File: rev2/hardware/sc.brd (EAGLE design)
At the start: 65 x 56 mm, 81 parts, among them IC1 PB137ACV, IC2 LM2675M-ADJ, Q1 si2305cd, Q2 IRFR5305, Q3 IRFR5305, T1 BC846, U1 SPX5205 3v3, X3 MKDSN1,5/4-5,08, X4 ts, X5 i2c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

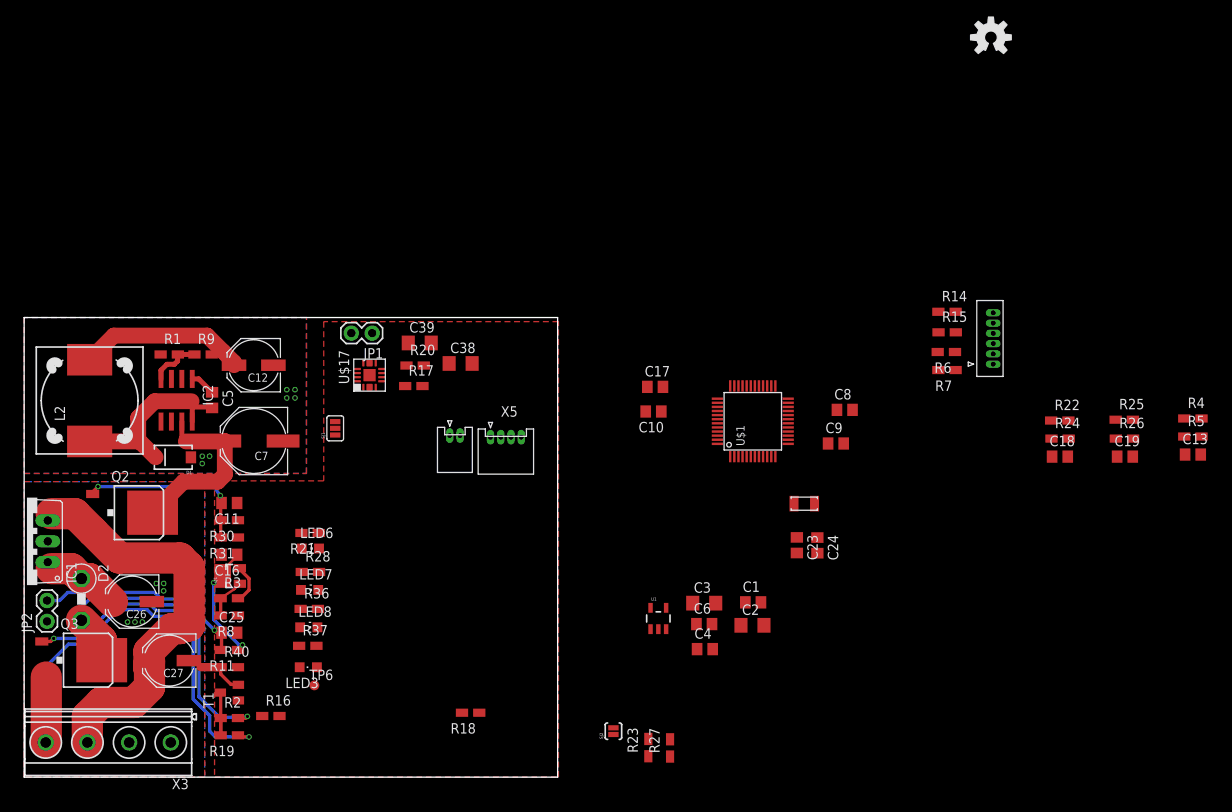
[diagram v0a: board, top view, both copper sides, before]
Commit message: rev2 routing 2/3
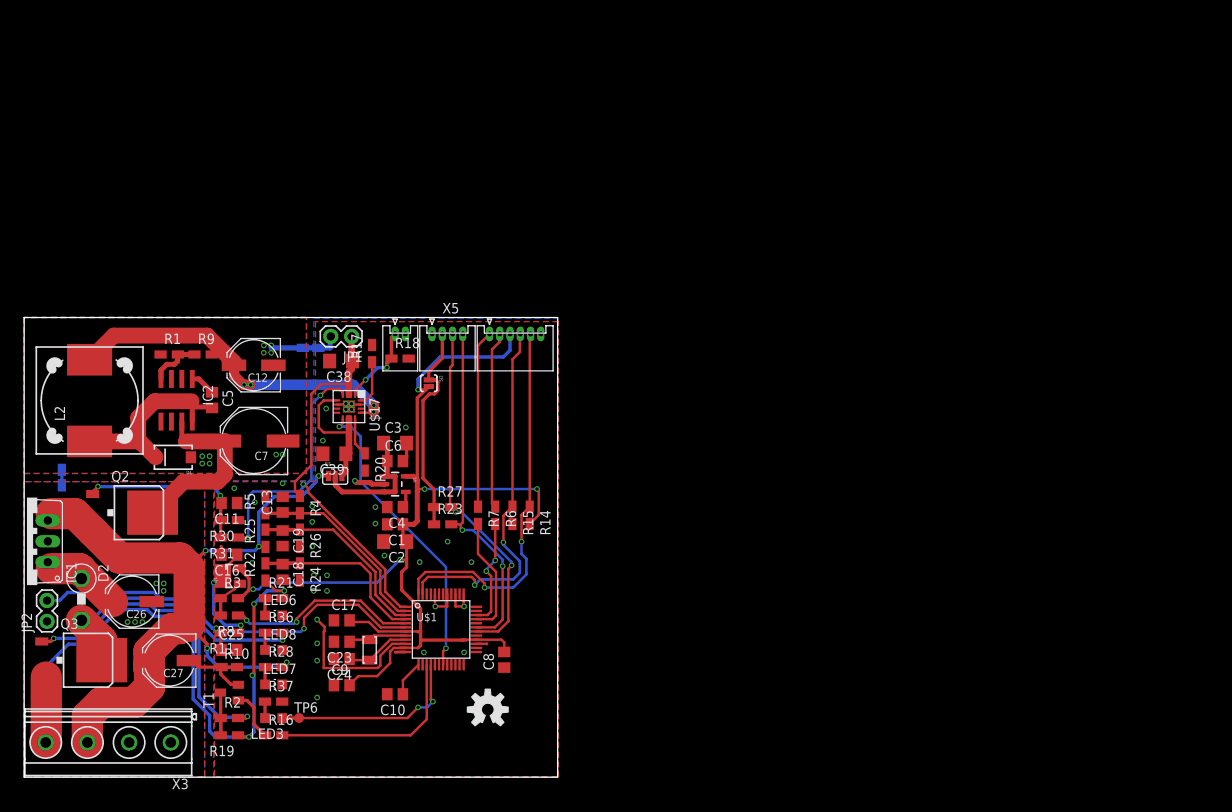
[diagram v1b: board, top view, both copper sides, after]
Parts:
- removed R40: 0R, rcl:R0805W
- removed X7: prog, Simplex-Connectors:0530470610
- added R10, R12, R13: 0R_0805, Simplex-Jumpers:R0805W
- added X1: prog, Simplex-Connectors:0530480610
- moved R5 113.3 mm to (29.4, 33.2), turned to 90 degrees
- moved C13 111.1 mm to (31.5, 33.2), turned to 90 degrees
- moved R4 109.3 mm to (33.6, 33.2), turned to 270 degrees
- moved R25 105.6 mm to (29.4, 29.1), turned to 90 degrees
- moved C19 103.1 mm to (31.5, 29.1), turned to 270 degrees
- moved U$7 102.3 mm to (56.5, 8.23)
- moved R26 101.2 mm to (33.6, 29.1), turned to 270 degrees
- moved R22 98.5 mm to (29.4, 25.0), turned to 90 degrees
- moved C18 95.7 mm to (31.5, 25.0), turned to 270 degrees
- moved R24 94.0 mm to (33.6, 25.0), turned to 270 degrees
- moved C9 67.0 mm to (38.7, 11.2)
- moved R7 59.8 mm to (55.3, 31.9), turned to 270 degrees
- moved C24 59.6 mm to (38.7, 14.4), turned to 180 degrees
- moved R6 58.5 mm to (57.4, 31.9), turned to 270 degrees
- moved R15 57.5 mm to (59.5, 31.9), turned to 270 degrees
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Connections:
- net +3V3: now also X1.3; no longer X7.3
- net BAT_DIV: now also U$1.2; no longer U$1.3
- net CE: now also U$1.1
- net GND: now also LED6.C, LED7.C, LED8.C, R10.2, R12.2, R13.1, R13.2, X1.6; no longer R40.2, X7.6
- net PV_DIV: now also U$1.4; no longer U$1.2
- net PV_EN: now also U$1.15; no longer U$1.22
- net RST: now also X1.5; no longer X7.5
- net RX: now also X1.2; no longer X7.2
- net STATUS: now also U$1.16; no longer U$1.36
- net TEST: now also X1.4; no longer X7.4
- net THERM: now also U$1.6; no longer U$1.5
- net TH_EN: now also U$1.5; no longer U$1.21
- net TX: now also X1.1; no longer X7.1
- net VBAT_DIV: now also U$1.3; no longer U$1.1
- net VBAT_GND: now also R10.1, R12.1; no longer LED6.C, LED7.C, LED8.C, R40.1
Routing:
- net +3V3: track 4.89 -> 133.5 mm, vias 0 -> 5
- net CE: track 0.00 -> 50.1 mm, vias 0 -> 3
- net GND: track 0.00 -> 48.5 mm, vias 7 -> 43
- net RST: track 0.00 -> 47.1 mm, vias 0 -> 2
- net TEST: track 0.00 -> 45.7 mm, vias 0 -> 2
- net SDA: track 0.00 -> 43.2 mm, vias 0 -> 2
- net SCL: track 0.00 -> 42.5 mm, vias 0 -> 2
- net VBAT: track 52.7 -> 93.7 mm, vias 0 -> 5
- net CHG: track 0.00 -> 36.5 mm, vias 0 -> 2
- net THERM: track 25.8 -> 52.3 mm, vias 1 -> 2
- net N$17: track 0.00 -> 26.5 mm
- net BAT: track 0.00 -> 26.3 mm
- net BAT_DIV: track 0.00 -> 25.9 mm
- net VBAT_DIV: track 0.00 -> 25.2 mm
- net PV+: track 59.0 -> 84.2 mm, vias 1 -> 4
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
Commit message: board ready
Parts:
- added C14: 100nF, rcl:C0805
- added R29: 470, rcl:R0805W
- added R32: 100k, rcl:R0805W
- added T2, T3: BC846, transistor:SOT23
- C11: value 1uF -> 10nF
- R19: value 10k -> 220k
- R3: value 100k -> 220k
- R30: value 1M -> 220k
- R31: value 10k -> 1M
- SJ1: value JUMPER-PAD-3-2OF3_NC_BY_PASTE -> sel_in
- SJ2: value JUMPER-PAD-2-NC_BY_PASTE -> i2c_pwr
- moved C18 4.66 mm to (36.0, 23.8)
- moved R30 4.60 mm to (25.1, 26.7)
- moved C13 4.56 mm to (35.9, 32.0)
- moved C19 4.56 mm to (35.9, 27.9)
- moved R25 4.56 mm to (33.8, 27.9)
- moved R26 4.56 mm to (38.0, 27.9)
- moved R4 4.56 mm to (38.0, 32.0)
- moved R5 4.56 mm to (33.8, 32.0)
- moved R22 4.56 mm to (33.8, 23.8)
- moved R24 4.56 mm to (38.0, 23.8)
- moved C16 2.80 mm to (25.1, 24.3)
- moved C25 2.80 mm to (25.1, 12.7)
- moved LED6 2.80 mm to (30.5, 16.9)
- moved LED7 2.80 mm to (30.5, 8.50)
- moved LED8 2.80 mm to (30.5, 12.7)
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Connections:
- new net N$20: R29.2, U$1.1
- new net N$22: C14.1, R31.1, T2.1, T3.3
- new net N$23: R32.1, T3.1
- net CE: now also R29.1, R32.2; no longer R31.1, U$1.1
- net GND: now also C14.2, T2.2, T3.2; no longer C11.1, R30.1
- net N$16: now also R30.1, T2.3; no longer R30.2, R31.2
- net N$49: now also C11.1
- net VBAT: now also R30.2, R31.2
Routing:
- net CE: track 50.1 -> 26.4 mm
- net N$16: track 21.8 -> 34.8 mm
- net N$20: track 0.00 -> 12.4 mm
- net N$22: track 0.00 -> 10.4 mm, vias 0 -> 2
- net GND: track 48.5 -> 57.1 mm, vias 43 -> 55
- net VBAT: track 93.7 -> 100.8 mm, vias 5 -> 6
- net STATUS: track 23.8 -> 30.6 mm
- net PV_DIV: track 23.8 -> 17.1 mm
- net N$49: track 22.2 -> 27.8 mm
- net VBAT_DIV: track 25.2 -> 20.1 mm
- net THERM: track 52.3 -> 57.0 mm
- net BAT_DIV: track 25.9 -> 21.4 mm
- net PV+: track 84.2 -> 88.4 mm, vias 4 -> 2
- net BAT: track 26.3 -> 29.6 mm
- net N$23: track 0.00 -> 3.23 mm
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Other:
- board text added: "+3v7"
- board text added: "Petre Rodan 201511 rev1"
- board text added: "bat"
- board text added: "github.com/rodan/solar-charger"
- board text added: "gnd"
- board text added: "i2c"
- board text added: "prog"
- board text added: "pv"
- board text added: "ts"
